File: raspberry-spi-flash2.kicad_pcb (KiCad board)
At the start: 2 copper layers, 65 x 56 mm, 60 parts, among them J3 40HAT, J9 CONN_01X02, Q1 BSS138, Q2 BSS138, Q4 BSS138, Q5 BSS138, SW1 SW_SPDT, SW2 SW_SPDT, U1 TXB0104D, U2 CAT24C32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

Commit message: Added jumper to work with Rock64 board which lacks CS1.
Signed-off-by: Aaron Williams <aaron.w2@gmail.com>
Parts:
- added J1: Conn_01x03, Pin_Headers:Pin_Header_Straight_1x03_Pitch2.54mm, F.Cu at (122.7, 74.5)
- moved C10 4.30 mm to (122.1, 71.9)
- moved R3 3.97 mm to (119.2, 76.6)
- moved Q1 3.69 mm to (128.0, 80.9)
- moved Q2 3.69 mm to (124.4, 80.9)
- moved Q5 2.91 mm to (120.8, 80.9)
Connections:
- U6 pad 3: R_FL_CS1 -> Net-(J1-Pad2)
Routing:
- net R_FL_CS0: track 19.2 -> 32.0 mm, vias 2 -> 4
- net R_FL_CS1: track 26.7 -> 31.9 mm, vias 2 -> 1
- net Net-(J1-Pad2): track 0.00 -> 5.03 mm, vias 0 -> 1
- net Net-(Q2-Pad3): track 29.3 -> 25.4 mm
- net Net-(Q1-Pad3): track 35.6 -> 31.9 mm
- net V3_3_SEL: track 100.4 -> 96.7 mm
- net (no net): track 0.00 -> 3.43 mm
- net /SPI Flash Programmer/~OE: track 23.6 -> 20.7 mm
- net VPP: track 138.3 -> 137.0 mm
- net GND: track 71.2 -> 70.1 mm, vias 28 -> 29
- net OE: track 93.4 -> 92.4 mm
- net /SPI Flash Programmer/FL_CS1: track 51.4 -> 50.5 mm
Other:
- board text added: "PI ~PI"

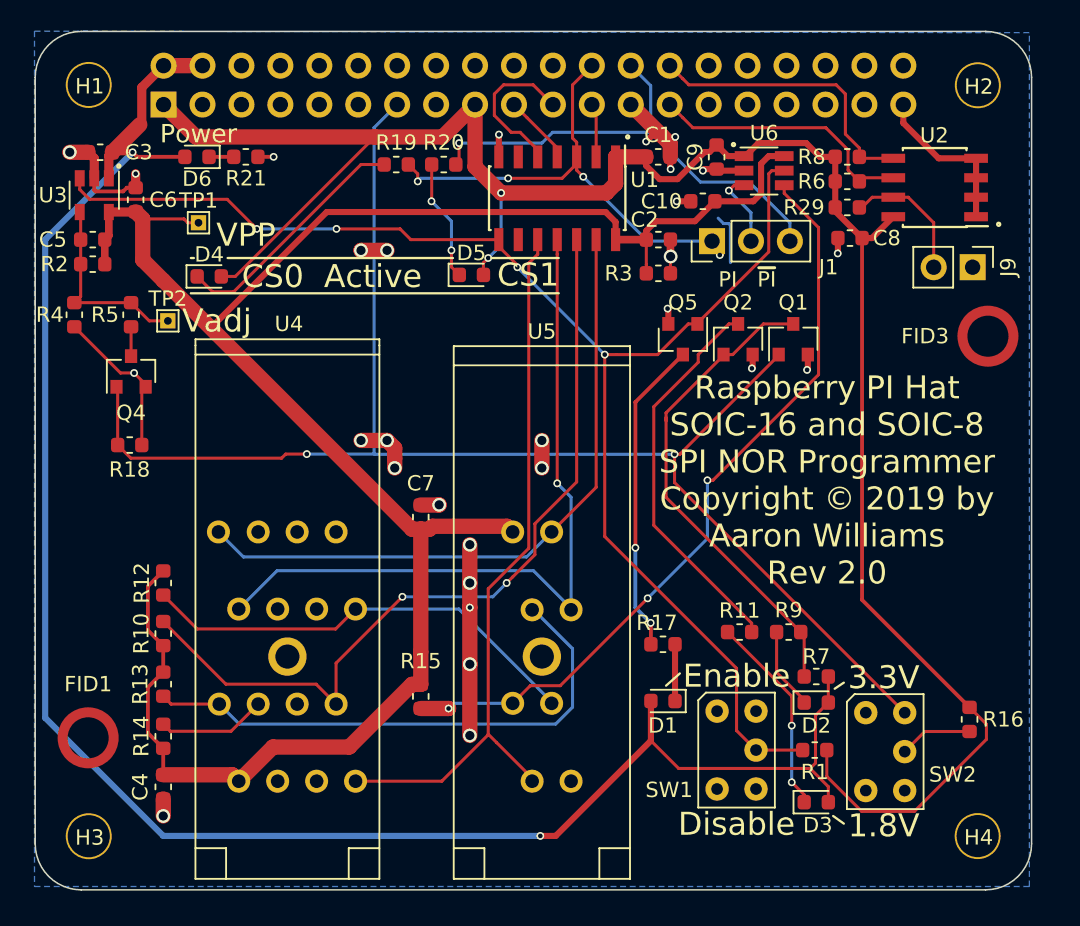
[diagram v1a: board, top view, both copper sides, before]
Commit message: Fixes a number of issues
This fixes a number of issues with the previous design.

1. The OE GPIO pin was not hooked up.
2. The level shifter has been changed to a 5 channel unidirectional
   level shifter.
3. LEDs were moved down near the base.
4. The switches were fixed based on measuring the contacts with different
   switch positions (not in the data sheet).
5. Added support for some non-Raspberry PI boards.
6. Changed resistors in power supply based on what is readily available.

Signed-off-by: Aaron Williams <aaron.w2@gmail.com>
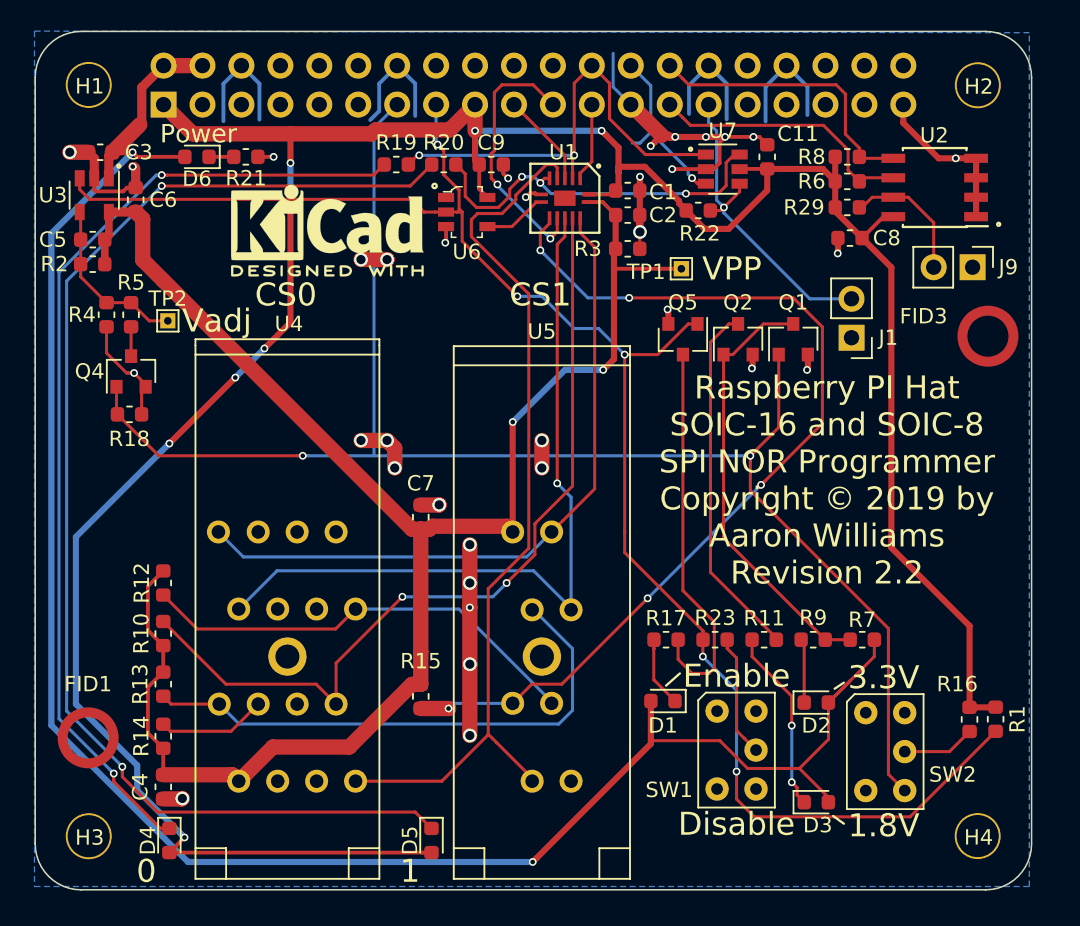
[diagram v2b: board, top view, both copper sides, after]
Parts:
- removed C10: 0.1uF, Capacitor_SMD:C_0603_1608Metric
- added A1: Logo-URL, Aaron:LOGO-raspberry-pi-spi-programmer2, B.Cu at (133.8, 94.0)
- added C11: 0.1uF, Capacitor_SMD:C_0603_1608Metric, F.Cu at (126.3, 69.0)
- added R22: 10K, Resistor_SMD:R_0603_1608Metric, F.Cu at (121.8, 72.5)
- added R23: 4.75K, Resistor_SMD:R_0603_1608Metric, F.Cu at (122.9, 100.5)
- added REF**: KiCad-Logo2_6mm_SilkScreen, Symbol:KiCad-Logo2_6mm_SilkScreen, F.Cu at (97.6, 73.8)
- added U7: SN74AUP1T157, Package_TO_SOT_SMD:SOT-23-6, F.Cu at (123.4, 69.8)
- J1: value Conn_01x03 -> Conn_01x02; footprint Pin_Headers:Pin_Header_Straight_1x03_Pitch2.54mm -> Connector_PinHeader_2.54mm:PinHeader_1x02_P2.54mm_Vertical
- R1: value 4.75K -> 1M
- R18: value 1M -> 100K
- R19: value 330 -> 560
- U1: value TXB0104D -> FXL5T244BQX; footprint Package_SO:SOIC-14_3.9x8.7mm_P1.27mm -> Aaron:DQFN-14-1EP_2.5x3mm_EP2.2x1.7mm_Thermal
- U6: value TXB0101DBV -> SN74LVC1G04DBVR; footprint Package_TO_SOT_SMD:TSOT-23-6 -> digikey-footprints:SOT-753
- moved D5 37.0 mm to (104.4, 113.6), turned to 270 degrees
- moved D4 36.9 mm to (87.3, 113.6), turned to 270 degrees
- moved TP1 31.6 mm to (120.7, 76.3)
- moved U6 19.6 mm to (106.7, 72.6), turned to 270 degrees
- moved C9 14.7 mm to (108.3, 69.5), turned to 0 degrees
- moved R1 12.0 mm to (141.2, 105.7), turned to 270 degrees
- moved J1 11.1 mm to (131.8, 80.8), turned to 180 degrees
- moved R7 3.84 mm to (132.5, 100.5)
- moved C1 2.96 mm to (117.2, 71.2)
- moved C2 2.56 mm to (117.2, 72.8)
- moved R3 2.56 mm to (117.2, 75.0)
- moved R4 2.10 mm to (83.2, 79.3)
- moved R18 2.00 mm to (84.7, 85.8)
- moved R9 1.68 mm to (129.3, 100.5)
- moved R11 1.68 mm to (126.1, 100.5)
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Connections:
- net /SPI Flash Programmer/ADJ renamed /SPI Flash Programmer/VPP_ADJ
- net /SPI Flash Programmer/FL_CS0 renamed /SPI Flash Programmer/~FL_CS0
- net Net-(R12-Pad2) renamed /SPI Flash Programmer/~WP
- net Net-(R13-Pad2) renamed /SPI Flash Programmer/~HOLD
- net V1_8_SEL renamed Net-(J3-Pad11)
- J1 pad 1: R_FL_CS0 -> GND
- J1 pad 2: Net-(J1-Pad2) -> CS1_CS0_SEL
- J3 pad 15: /OE -> OE
- J3 pad 29: Net-(J3-Pad29) -> CS1_CS0_SEL
- Q5 pad 3: /SPI Flash Programmer/~OE -> Net-(Q5-Pad3)
- R15 pad 2: /SPI Flash Programmer/FL_CS1 -> /SPI Flash Programmer/~FL_CS1
- R17 pad 2: /SPI Flash Programmer/~OE -> Net-(Q5-Pad3)
- R20 pad 2: R_FL_CS1 -> /SPI Flash Programmer/MUX_FL_CS1
- SW1 pad 1: Net-(SW1-Pad1) -> GND
- SW1 pad 2: OE -> Net-(R23-Pad2)
- SW1 pad 3: GND -> Net-(SW1-Pad3)
- SW2 pad 1: V3_3_SEL -> Net-(SW2-Pad1)
- SW2 pad 3: Net-(SW2-Pad3) -> V3_3_SEL
- U1 pad 10: /SPI Flash Programmer/MISO -> R_MISO
- U1 pad 5: R_MISO -> /SPI Flash Programmer/MISO
- U1 pad 6: Net-(U1-Pad6) -> /SPI Flash Programmer/MUX_FL_CS1
- U1 pad 8: OE -> /SPI Flash Programmer/~OE
- U1 pad 9: Net-(U1-Pad9) -> /SPI Flash Programmer/~FL_CS1
- U5 pad 1: /SPI Flash Programmer/FL_CS1 -> /SPI Flash Programmer/~FL_CS1
- U6 pad 1: +3V3 -> Net-(U6-Pad1)
- U6 pad 2: GND -> OE
- U6 pad 3: Net-(J1-Pad2) -> GND
- U6 pad 4: /SPI Flash Programmer/FL_CS1 -> /SPI Flash Programmer/~OE
- U6 pad 5: OE -> +3V3
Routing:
- net Net-(D5-Pad1): track 7.96 -> 82.4 mm
- net /SPI Flash Programmer/~FL_CS1: track 0.00 -> 63.0 mm, vias 0 -> 5
- net /SPI Flash Programmer/FL_CS1: track 50.5 -> 0.00 mm, vias 3 -> 0
- net Net-(D4-Pad1): track 16.1 -> 63.7 mm, vias 0 -> 2
- net +3V3: track 135.1 -> 182.6 mm, vias 2 -> 8
- net GND: track 70.1 -> 113.3 mm, vias 29 -> 34
- net Net-(Q5-Pad3): track 0.00 -> 25.5 mm
- net /SPI Flash Programmer/MUX_FL_CS1: track 0.00 -> 24.8 mm, vias 0 -> 3
- net CS1_CS0_SEL: track 0.00 -> 21.1 mm, vias 0 -> 1
- net R_FL_CS1: track 31.9 -> 11.5 mm
- net VPP: track 137.0 -> 117.1 mm, vias 0 -> 2
- net /SPI Flash Programmer/~OE: track 20.7 -> 3.86 mm, vias 2 -> 0
- net OE: track 92.4 -> 107.1 mm, vias 4 -> 5
- net /SPI Flash Programmer/MISO: track 47.6 -> 58.3 mm
- net Net-(R23-Pad2): track 0.00 -> 7.98 mm
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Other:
- board text added: "0"
- board text added: "1"
- board text added: "CS0"
- board text added: "Install J1 enables both sockets to use CS0. It is only required if not running on a Raspberry PI and software doesn't control the CS1 mux. If not running on a Raspberry PI DO NOT install devices in both sockets at the same time."
- board text added: "Raspberry PI Hat SOIC-16 and SOIC-8 SPI NOR Programmer Copyright © 2019 by Aaron Williams Revision 2.2"
- board text removed: "CS0 Active"
- board text removed: "PI ~PI"
- board text removed: "Raspberry PI Hat SOIC-16 and SOIC-8 SPI NOR Programmer Copyright © 2019 by Aaron Williams Rev 2.0"

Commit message: Fixed solder mask setting and minor cleanups
Signed-off-by: aaronw <aaron.w2@gmail.com>
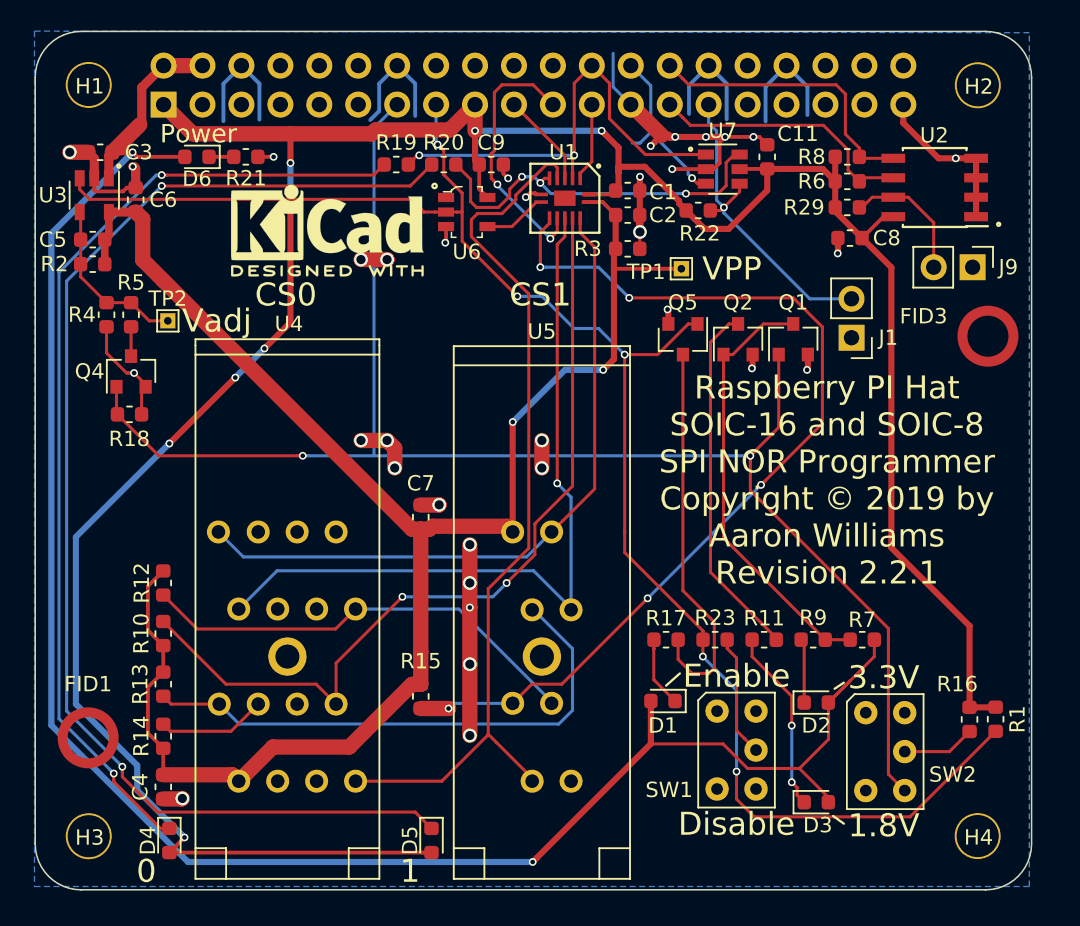
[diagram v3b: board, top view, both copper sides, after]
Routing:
- net /SPI Flash Programmer/~FL_CS1: track 63.0 -> 63.7 mm
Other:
- rule pad_to_mask_clearance: -0.0508 -> 0.0508
- board text added: "Raspberry PI Hat SOIC-16 and SOIC-8 SPI NOR Programmer Copyright © 2019 by Aaron Williams Revision 2.2.1"
- board text removed: "Raspberry PI Hat SOIC-16 and SOIC-8 SPI NOR Programmer Copyright © 2019 by Aaron Williams Revision 2.2"
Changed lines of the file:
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@@
     (thickness 1.6)
     (drawings 73)
-    (tracks 657)
+    (tracks 658)
     (zones 0)
     (modules 66)
@@
   (title_block
     (title "Raspberry Pi SPI NOR Programmer Hat")
-    (date 2019-01-28)
-    (rev 2.2.0)
+    (date 2019-02-08)
+    (rev 2.2.1)
   )
   (layers
@@
     (pad_size 2.5 2.5)
     (pad_drill 1.57)
-    (pad_to_mask_clearance -0.0508)
+    (pad_to_mask_clearance 0.0508)
     (solder_mask_min_width 0.25)
     (aux_axis_origin 0 0)
@@
       (plotvalue false)
       (plotinvisibletext false)
-      (padsonsilk true)
+      (padsonsilk false)
       (subtractmaskfromsilk false)
       (outputformat 1)
@@
     (effects (font (size 1.5 1.5) (thickness 0.3)))
   )
-  (gr_text "Raspberry PI Hat\nSOIC-16 and SOIC-8\nSPI NOR Programmer\nCopyright © 2019 by\nAaron Williams\nRevision 2.2" (at 130.2 90.1) (layer F.SilkS)
+  (gr_text "Raspberry PI Hat\nSOIC-16 and SOIC-8\nSPI NOR Programmer\nCopyright © 2019 by\nAaron Williams\nRevision 2.2.1" (at 130.2 90.1) (layer F.SilkS)
     (effects (font (size 1.5 1.5) (thickness 0.3)))
   )
@@
   (segment (start 106.075 72.6) (end 106.4 72.6) (width 0.2) (layer F.Cu) (net 29))
   (segment (start 106.4 74.5) (end 106.4 72.6) (width 0.2) (layer F.Cu) (net 29))
-  (segment (start 105.2 68.6) (end 105.054999 68.454999) (width 0.2) (layer F.Cu) (net 29))
-  (segment (start 105.054999 68.454999) (end 104.8 68.2) (width 0.2) (layer F.Cu) (net 29))
-  (segment (start 105.2 70.1657) (end 105.2 68.6) (width 0.2) (layer F.Cu) (net 29))
-  (segment (start 106.199989 71.165689) (end 105.2 70.1657) (width 0.2) (layer F.Cu) (net 29))
-  (segment (start 106.199989 72.399989) (end 106.199989 71.165689) (width 0.2) (layer F.Cu) (net 29))
-  (segment (start 106.4 72.6) (end 106.199989 72.399989) (width 0.2) (layer F.Cu) (net 29))
   (segment (start 103.9 72.6) (end 104.625 72.6) (width 0.2) (layer F.Cu) (net 29))
   (segment (start 104.625 72.6) (end 105.35 72.6) (width 0.2) (layer F.Cu) (net 29))
@@
   (segment (start 81.45 70.4) (end 81.45 71.13) (width 0.2) (layer F.Cu) (net 29))
   (segment (start 81.45 71.13) (end 82.089999 71.769999) (width 0.2) (layer F.Cu) (net 29))
+  (segment (start 105.054999 68.454999) (end 104.8 68.2) (width 0.2) (layer F.Cu) (net 29))
+  (segment (start 105.2 68.6) (end 105.054999 68.454999) (width 0.2) (layer F.Cu) (net 29))
+  (segment (start 105.2 70.1657) (end 105.2 68.6) (width 0.2) (layer F.Cu) (net 29))
+  (segment (start 106.4 72.6) (end 106.4 71.3657) (width 0.2) (layer F.Cu) (net 29))
+  (segment (start 106.4 71.3657) (end 105.2 70.1657) (width 0.2) (layer F.Cu) (net 29))
   (segment (start 85.369999 66.905001) (end 83.575 68.7) (width 1) (layer F.Cu) (net 30) (status 20))
   (segment (start 83.35 68.925) (end 83.575 68.7) (width 0.6) (layer F.Cu) (net 30) (status 30))
@@
   (segment (start 133.2875 101.6) (end 130.2875 104.6) (width 0.2) (layer F.Cu) (net 30))
   (segment (start 133.2875 100.5) (end 133.2875 101.6) (width 0.2) (layer F.Cu) (net 30))
-  (segment (start 123.208904 107.0875) (end 118.7125 107.0875) (width 0.2) (layer F.Cu) (net 30))
-  (segment (start 128.4 108.9) (end 125.021404 108.9) (width 0.2) (layer F.Cu) (net 30))
-  (segment (start 125.021404 108.9) (end 123.208904 107.0875) (width 0.2) (layer F.Cu) (net 30))
   (segment (start 118.7125 107.0875) (end 118.7125 107.2875) (width 0.4) (layer F.Cu) (net 30))
   (via (at 111 115) (size 0.51) (drill 0.3) (layers F.Cu B.Cu) (net 30))
@@
   (segment (start 84.9 68.7) (end 79.599971 74.000029) (width 0.4) (layer B.Cu) (net 30))
   (segment (start 79.599971 74.000029) (end 79.599971 106.081002) (width 0.4) (layer B.Cu) (net 30))
+  (segment (start 118.725 107.3) (end 118.7125 107.2875) (width 0.2) (layer F.Cu) (net 30))
+  (segment (start 123.421404 107.3) (end 118.725 107.3) (width 0.2) (layer F.Cu) (net 30))
+  (segment (start 128.4 108.9) (end 125.021404 108.9) (width 0.2) (layer F.Cu) (net 30))
+  (segment (start 125.021404 108.9) (end 123.421404 107.3) (width 0.2) (layer F.Cu) (net 30))
   (segment (start 114.1 70.07) (end 114.1 70.4) (width 0.2) (layer F.Cu) (net 31))
   (segment (start 114.86 69.31) (end 114.1 70.07) (width 0.2) (layer F.Cu) (net 31))
@@
   (segment (start 111.100016 70.3) (end 110.660624 70.3) (width 0.2) (layer B.Cu) (net 60))
   (segment (start 111.5 70.699984) (end 111.100016 70.3) (width 0.2) (layer B.Cu) (net 60))
+  (via (at 110.3 70.3) (size 0.51) (drill 0.3) (layers F.Cu B.Cu) (net 60))
   (segment (start 110.045001 70.554999) (end 110.3 70.3) (width 0.2) (layer F.Cu) (net 60))
   (segment (start 109.5 71.1) (end 110.045001 70.554999) (width 0.2) (layer F.Cu) (net 60))
-  (segment (start 109.5 71.565002) (end 109.5 71.1) (width 0.2) (layer F.Cu) (net 60))
-  (via (at 110.3 70.3) (size 0.51) (drill 0.3) (layers F.Cu B.Cu) (net 60))
+  (segment (start 106.95 70.4625) (end 106.95 71.915002) (width 0.2) (layer F.Cu) (net 60))
+  (segment (start 105.9875 69.5) (end 106.95 70.4625) (width 0.2) (layer F.Cu) (net 60))
+  (segment (start 106.95 71.915002) (end 107.334998 72.3) (width 0.2) (layer F.Cu) (net 60))
   (segment (start 107.334998 72.3) (end 108.765002 72.3) (width 0.2) (layer F.Cu) (net 60))
-  (segment (start 106.6 71.565002) (end 107.334998 72.3) (width 0.2) (layer F.Cu) (net 60))
   (segment (start 108.765002 72.3) (end 109.5 71.565002) (width 0.2) (layer F.Cu) (net 60))
-  (segment (start 105.9875 69.5) (end 106.6 70.1125) (width 0.2) (layer F.Cu) (net 60))
-  (segment (start 106.6 70.1125) (end 106.6 71.565002) (width 0.2) (layer F.Cu) (net 60))
+  (segment (start 109.5 71.565002) (end 109.5 71.1) (width 0.2) (layer F.Cu) (net 60))
   (segment (start 89.1125 99.8) (end 86.9 97.5875) (width 0.2) (layer F.Cu) (net 61) (status 20))
   (segment (start 99.445 98.5) (end 98.145 99.8) (width 0.2) (layer F.Cu) (net 61) (status 10))
@@
   (segment (start 105.767496 104.732504) (end 105.512497 104.987503) (width 0.2) (layer B.Cu) (net 62))
   (via (at 117.3 78.2) (size 0.51) (drill 0.3) (layers F.Cu B.Cu) (net 62))
-  (segment (start 117.3 78.2) (end 114.600002 78.2) (width 0.2) (layer B.Cu) (net 62))
-  (segment (start 111.754999 75.354997) (end 111.5 75.099998) (width 0.2) (layer B.Cu) (net 62))
-  (via (at 111.5 75.099998) (size 0.51) (drill 0.3) (layers F.Cu B.Cu) (net 62))
-  (segment (start 114.600002 78.2) (end 111.754999 75.354997) (width 0.2) (layer B.Cu) (net 62))
   (via (at 125.9 90.399994) (size 0.51) (drill 0.3) (layers F.Cu B.Cu) (net 62))
   (segment (start 118.5 97.8) (end 125.9 90.4) (width 0.2) (layer B.Cu) (net 62))
@@
   (segment (start 109.695 104.65) (end 110.945 103.4) (width 0.2) (layer F.Cu) (net 62))
   (segment (start 110.945 103.4) (end 112.9 103.4) (width 0.2) (layer F.Cu) (net 62))
-  (segment (start 111.5 73.95) (end 111.5 75.099998) (width 0.2) (layer F.Cu) (net 62))
-  (segment (start 112.1 73) (end 112.1 73.35) (width 0.2) (layer F.Cu) (net 62))
-  (segment (start 112.1 73.35) (end 111.5 73.95) (width 0.2) (layer F.Cu) (net 62))
+  (via (at 111.5 76.2) (size 0.51) (drill 0.3) (layers F.Cu B.Cu) (net 62))
+  (segment (start 117.3 78.2) (end 115.3 76.2) (width 0.2) (layer B.Cu) (net 62))
+  (segment (start 111.5 73.93) (end 111.5 75.839376) (width 0.2) (layer F.Cu) (net 62))
+  (segment (start 112.1 73.33) (end 111.5 73.93) (width 0.2) (layer F.Cu) (net 62))
+  (segment (start 112.1 73) (end 112.1 73.33) (width 0.2) (layer F.Cu) (net 62))
+  (segment (start 111.5 75.839376) (end 111.5 76.2) (width 0.2) (layer F.Cu) (net 62))
+  (segment (start 111.860624 76.2) (end 111.5 76.2) (width 0.2) (layer B.Cu) (net 62))
+  (segment (start 115.3 76.2) (end 111.860624 76.2) (width 0.2) (layer B.Cu) (net 62))
   (segment (start 87.4125 104.7) (end 86.9 104.1875) (width 0.2) (layer F.Cu) (net 63) (status 20))
   (segment (start 90.555 104.7) (end 87.4125 104.7) (width 0.2) (layer F.Cu) (net 63) (status 10))
